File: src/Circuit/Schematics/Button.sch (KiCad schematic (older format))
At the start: 5 parts

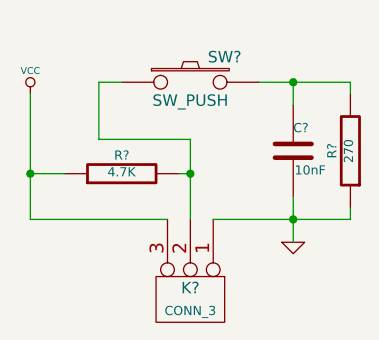
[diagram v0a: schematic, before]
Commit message: Moved debounce capacitor to behind the switch
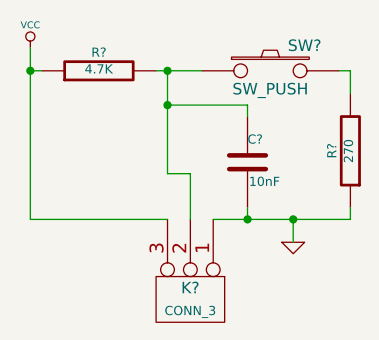
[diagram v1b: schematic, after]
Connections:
- net at K?.2 (PM), R?.2, SW?.1: now also C?.1
- net at R?.2, SW?.2: no longer C?.1
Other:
- moved on the sheet: C?, R?, SW?
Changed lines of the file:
@@
 Sheet 1 1
 Title "noname.sch"
-Date "5 dec 2014"
+Date "6 dec 2014"
 Rev ""
 Comp ""
@@
 L SW_PUSH SW?
 U 1 1 54819B65
-P 5450 4200
-F 0 "SW?" H 5600 4310 50  0000 C CNN
-F 1 "SW_PUSH" H 5450 4120 50  0000 C CNN
-F 2 "~" H 5450 4200 60  0000 C CNN
-F 3 "~" H 5450 4200 60  0000 C CNN
-	1    5450 4200
+P 5800 4150
+F 0 "SW?" H 5950 4260 50  0000 C CNN
+F 1 "SW_PUSH" H 5800 4070 50  0000 C CNN
+F 2 "~" H 5800 4150 60  0000 C CNN
+F 3 "~" H 5800 4150 60  0000 C CNN
+	1    5800 4150
 	1    0    0    -1
 $EndComp
@@
 L C C?
 U 1 1 54819BA6
-P 5900 4500
-F 0 "C?" H 5900 4600 40  0000 L CNN
-F 1 "10nF" H 5906 4415 40  0000 L CNN
-F 2 "~" H 5938 4350 30  0000 C CNN
-F 3 "~" H 5900 4500 60  0000 C CNN
-	1    5900 4500
+P 5700 4550
+F 0 "C?" H 5700 4650 40  0000 L CNN
+F 1 "10nF" H 5706 4465 40  0000 L CNN
+F 2 "~" H 5738 4400 30  0000 C CNN
+F 3 "~" H 5700 4550 60  0000 C CNN
+	1    5700 4550
 	1    0    0    -1
 $EndComp
@@
 	1    0    0    -1
 $EndComp
-Wire Wire Line
-	5900 4700 5900 4900
-Wire Wire Line
-	5750 4200 6150 4200
-Wire Wire Line
-	5900 4200 5900 4300
-Wire Wire Line
-	6150 4200 6150 4250
-Connection ~ 5900 4200
-Wire Wire Line
-	6150 4800 6150 4750
-Wire Wire Line
-	5550 4800 6150 4800
-Connection ~ 5900 4800
 $Comp
 L CONN_3 K?
@@
 	0    1    1    0
 $EndComp
-Wire Wire Line
-	4750 4800 5350 4800
 $Comp
 L R R?
 U 1 1 54819D40
-P 5150 4600
-F 0 "R?" V 5230 4600 40  0000 C CNN
-F 1 "4.7K" V 5157 4601 40  0000 C CNN
-F 2 "~" V 5080 4600 30  0000 C CNN
-F 3 "~" H 5150 4600 30  0000 C CNN
-	1    5150 4600
+P 5050 4150
+F 0 "R?" V 5130 4150 40  0000 C CNN
+F 1 "4.7K" V 5057 4151 40  0000 C CNN
+F 2 "~" V 4980 4150 30  0000 C CNN
+F 3 "~" H 5050 4150 30  0000 C CNN
+	1    5050 4150
 	0    -1   -1   0
 $EndComp
-Wire Wire Line
-	4750 4600 4900 4600
-Wire Wire Line
-	5400 4600 5450 4600
-Connection ~ 5450 4600
-Wire Wire Line
-	5450 4450 5450 4800
-Wire Wire Line
-	5050 4450 5450 4450
-Wire Wire Line
-	5050 4450 5050 4200
-Wire Wire Line
-	5050 4200 5150 4200
-Wire Wire Line
-	4750 4800 4750 4250
-Connection ~ 4750 4600
 $Comp
 L VCC #PWR?
 U 1 1 5481A581
-P 4750 4250
-F 0 "#PWR?" H 4750 4350 30  0001 C CNN
-F 1 "VCC" H 4750 4350 30  0000 C CNN
-F 2 "~" H 4750 4250 60  0000 C CNN
-F 3 "~" H 4750 4250 60  0000 C CNN
-	1    4750 4250
+P 4750 4050
+F 0 "#PWR?" H 4750 4150 30  0001 C CNN
+F 1 "VCC" H 4750 4150 30  0000 C CNN
+F 2 "~" H 4750 4050 60  0000 C CNN
+F 3 "~" H 4750 4050 60  0000 C CNN
+	1    4750 4050
 	1    0    0    -1
 $EndComp
+Wire Wire Line
+	6150 4150 6150 4250
+Wire Wire Line
+	6150 4800 6150 4750
+Wire Wire Line
+	5550 4800 6150 4800
+Wire Wire Line
+	4750 4800 5350 4800
+Wire Wire Line
+	4750 4050 4750 4800
+Wire Wire Line
+	5900 4800 5900 4900
+Connection ~ 5900 4800
+Wire Wire Line
+	5450 4600 5450 4800
+Wire Wire Line
+	5350 4150 5350 4600
+Wire Wire Line
+	5300 4150 5500 4150
+Wire Wire Line
+	5350 4300 5700 4300
+Wire Wire Line
+	5700 4300 5700 4350
+Connection ~ 5350 4300
+Wire Wire Line
+	5700 4750 5700 4800
+Connection ~ 5700 4800
+Wire Wire Line
+	6100 4150 6150 4150
+Wire Wire Line
+	4800 4150 4750 4150
+Connection ~ 4750 4150
+Connection ~ 5350 4150
+Wire Wire Line
+	5350 4600 5450 4600
 $EndSCHEMATC
